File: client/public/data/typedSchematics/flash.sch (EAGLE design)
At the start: 2 parts, among them IC1 M25P80VMN6TPBA

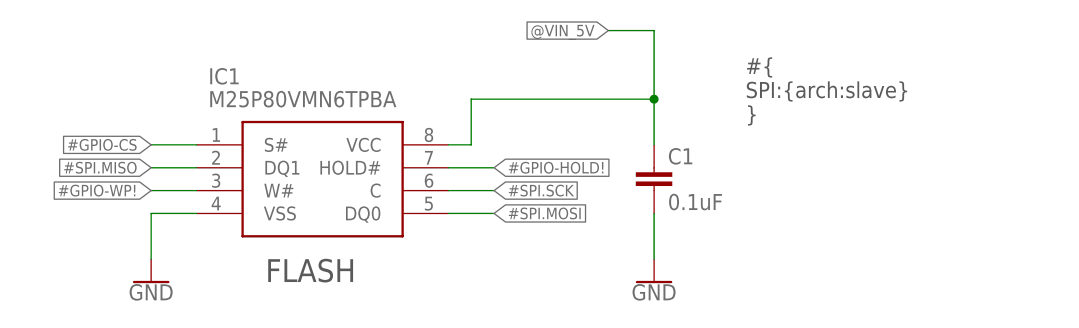
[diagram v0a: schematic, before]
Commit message: Configuring schematics with blocktype info
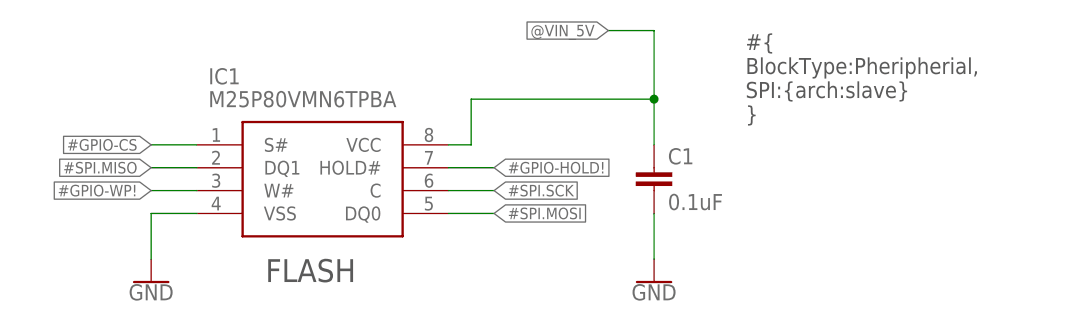
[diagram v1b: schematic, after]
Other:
- note added: "#{ BlockType:Pheripherial, SPI:{arch:slave} }"
- note removed: "#{ SPI:{arch:slave} }"
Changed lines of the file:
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@@
 <text x="30.48" y="7.62" size="2.54" layer="97">FLASH</text>
 <text x="83.82" y="25.4" size="1.778" layer="97">#{
+BlockType:Pheripherial,
 SPI:{arch:slave}
 }</text>
